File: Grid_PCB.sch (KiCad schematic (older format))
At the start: 9 parts, among them J10 LED_Conn, J11 ESP_Conn, J9 ESP_Conn, U1 SN74HC151N

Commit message: minor fix to mux strobe (enable) pin
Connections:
- net GND: now also U1.7 (~G)
- no-connect marks 2 -> 1
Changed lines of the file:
@@
 Wire Wire Line
 	4150 1500 4650 1500
-$Comp
-L grid:SN74HC151N U1
-U 1 1 61544325
-P 5500 4900
-F 0 "U1" H 5500 5475 50  0000 C CNN
-F 1 "SN74HC151N" H 5500 5384 50  0000 C CNN
-F 2 "Package_DIP:DIP-16_W10.16mm" H 5550 4900 50  0001 C CNN
-F 3 "https://www.ti.com/lit/ds/symlink/sn74hc151.pdf?ts=1632846774937&ref_url=https%253A%252F%252Fwww.google.com%252F" H 5550 4900 50  0001 C CNN
-	1    5500 4900
-	1    0    0    -1
-$EndComp
 Text Label 4800 4750 0    50   ~ 0
 BTN1
@@
 	1    0    0    -1
 $EndComp
-NoConn ~ 5200 5150
 $Comp
 L Device:C C9
@@
 	1    0    0    -1
 $EndComp
+$Comp
+L grid:SN74HC151N U1
+U 1 1 61544325
+P 5500 4900
+F 0 "U1" H 5500 5475 50  0000 C CNN
+F 1 "SN74HC151N" H 5500 5384 50  0000 C CNN
+F 2 "Package_DIP:DIP-16_W10.16mm" H 5550 4900 50  0001 C CNN
+F 3 "https://www.ti.com/lit/ds/symlink/sn74hc151.pdf?ts=1632846774937&ref_url=https%253A%252F%252Fwww.google.com%252F" H 5550 4900 50  0001 C CNN
+	1    5500 4900
+	1    0    0    -1
+$EndComp
+Wire Wire Line
+	5200 5150 5100 5150
+Wire Wire Line
+	5100 5150 5100 5250
+Connection ~ 5100 5250
 $EndSCHEMATC

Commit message: updated conns and mounting holes
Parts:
- J10, J11: footprint Connector_JST:JST_EH_B2B-EH-A_1x02_P2.50mm_Vertical -> conn:TE_640456-2
- J9: footprint Connector_JST:JST_EH_B5B-EH-A_1x05_P2.50mm_Vertical -> conn:TE_640456-5
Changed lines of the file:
@@
 F 0 "J10" H 8558 5131 50  0000 C CNN
 F 1 "LED_Conn" H 8558 5040 50  0000 C CNN
-F 2 "Connector_JST:JST_EH_B2B-EH-A_1x02_P2.50mm_Vertical" H 8450 4950 50  0001 C CNN
+F 2 "conn:TE_640456-2" H 8450 4950 50  0001 C CNN
 F 3 "~" H 8450 4950 50  0001 C CNN
 	1    8450 4950
@@
 F 0 "J9" H 1658 5081 50  0000 C CNN
 F 1 "ESP_Conn" H 1658 4990 50  0000 C CNN
-F 2 "Connector_JST:JST_EH_B5B-EH-A_1x05_P2.50mm_Vertical" H 1550 4600 50  0001 C CNN
+F 2 "conn:TE_640456-5" H 1550 4600 50  0001 C CNN
 F 3 "~" H 1550 4600 50  0001 C CNN
 	1    1550 4600
@@
 F 0 "J11" H 1858 6281 50  0000 C CNN
 F 1 "ESP_Conn" H 1858 6190 50  0000 C CNN
-F 2 "Connector_JST:JST_EH_B2B-EH-A_1x02_P2.50mm_Vertical" H 1750 5800 50  0001 C CNN
+F 2 "conn:TE_640456-2" H 1750 5800 50  0001 C CNN
 F 3 "~" H 1750 5800 50  0001 C CNN
 	1    1750 5800

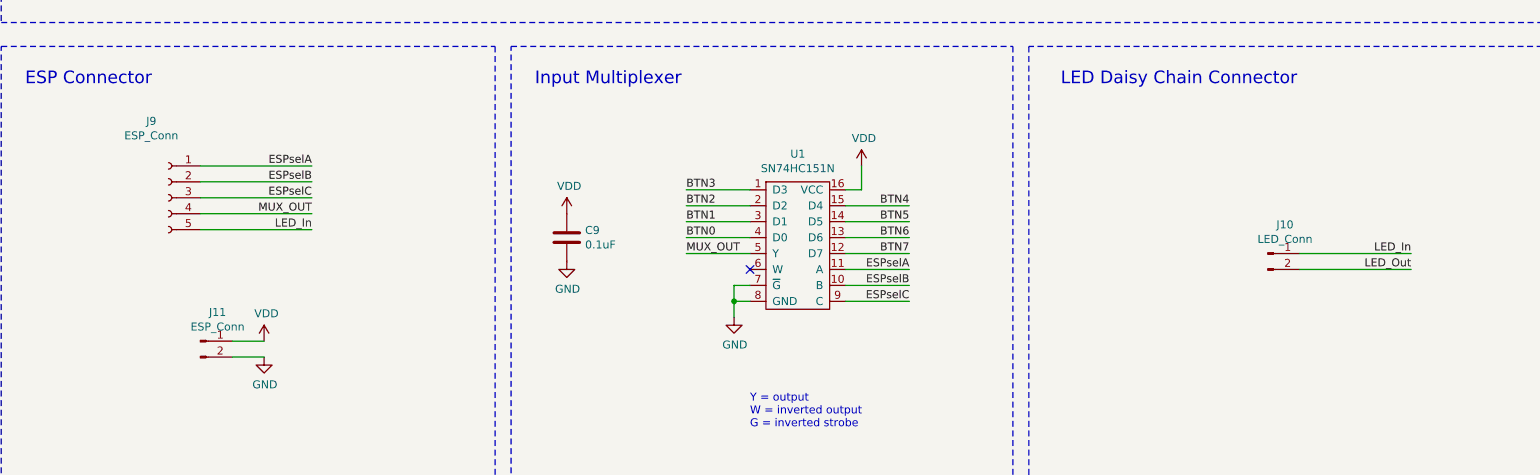
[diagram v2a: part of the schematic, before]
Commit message: updated jst footprint/library and updated routing on sel signals
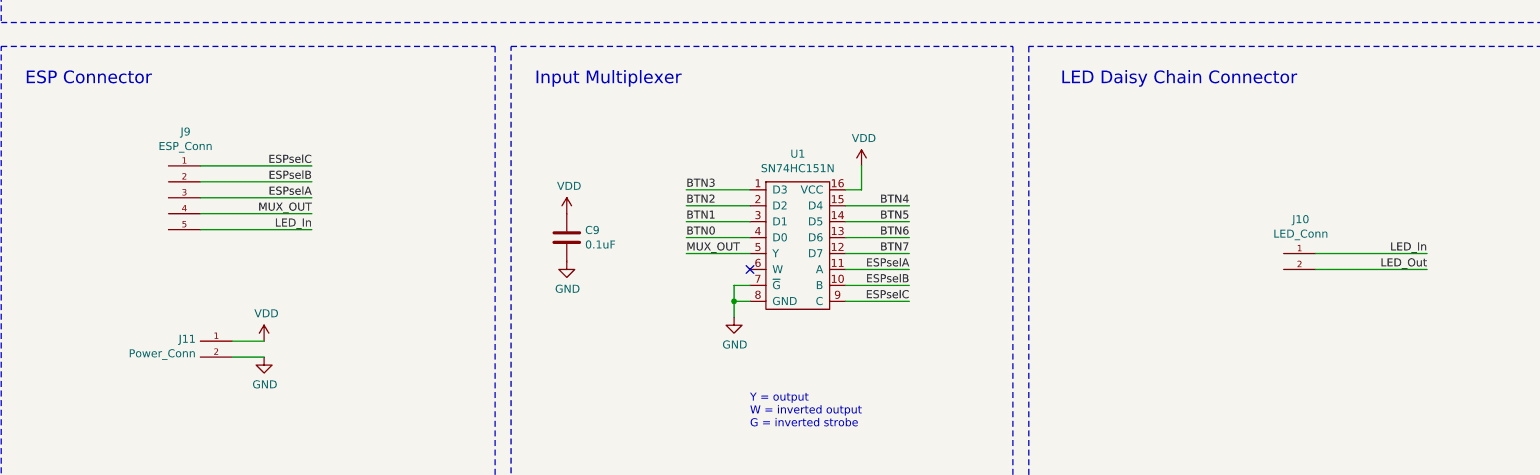
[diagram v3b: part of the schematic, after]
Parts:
- removed J10: LED_Conn, conn:TE_640456-2, symbol Connector:Conn_01x02_Male
- removed J11: ESP_Conn, conn:TE_640456-2, symbol grid:ESP_Conn
- removed J9: ESP_Conn, conn:TE_640456-5, symbol Connector:Conn_01x05_Female
- added J10: LED_Conn, JST_Conn:TE_640456-2, symbol JST_Conn:640456-2
- added J11: Power_Conn, JST_Conn:TE_640456-2, symbol JST_Conn:640456-2
- added J9: ESP_Conn, JST_Conn:TE_640456-5, symbol JST_Conn:640456-5
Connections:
- net ESPselA: now also J9.3
- net ESPselB: now also J9.2
- net ESPselC: now also J9.1
- net GND: now also J11.2
- net LED_In: now also J10.1, J9.5
- net LED_Out: now also J10.2
- net MUX_OUT: now also J9.4
- net VDD: now also J11.1
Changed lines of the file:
@@
 Text Label 2450 4700 2    50   ~ 0
 MUX_OUT
+Text Label 2450 4600 2    50   ~ 0
+ESPselA
 Text Label 2450 4400 2    50   ~ 0
-ESPselA
-Text Label 2450 4600 2    50   ~ 0
 ESPselC
 Text Label 2450 4500 2    50   ~ 0
 ESPselB
 Wire Wire Line
+	1750 4600 2450 4600
+Wire Wire Line
+	2450 4500 1750 4500
+Wire Wire Line
 	1750 4400 2450 4400
-Wire Wire Line
-	2450 4500 1750 4500
-Wire Wire Line
-	1750 4600 2450 4600
 Text Label 2450 4800 2    50   ~ 0
 LED_In
 Wire Wire Line
 	1750 4800 2450 4800
-$Comp
-L Connector:Conn_01x02_Male J10
-U 1 1 615862D5
-P 8450 4950
-F 0 "J10" H 8558 5131 50  0000 C CNN
-F 1 "LED_Conn" H 8558 5040 50  0000 C CNN
-F 2 "conn:TE_640456-2" H 8450 4950 50  0001 C CNN
-F 3 "~" H 8450 4950 50  0001 C CNN
-	1    8450 4950
-	1    0    0    -1
-$EndComp
-Wire Wire Line
-	8650 4950 9350 4950
-Text Label 9350 4950 2    50   ~ 0
+Wire Wire Line
+	8750 4950 9450 4950
+Text Label 9450 4950 2    50   ~ 0
 LED_In
 Wire Wire Line
-	8650 5050 9350 5050
-Text Label 9350 5050 2    50   ~ 0
+	8750 5050 9450 5050
+Text Label 9450 5050 2    50   ~ 0
 LED_Out
 Wire Wire Line
@@
 Wire Wire Line
 	1950 5600 2150 5600
-$Comp
-L Connector:Conn_01x05_Female J9
-U 1 1 6159E326
-P 1550 4600
-F 0 "J9" H 1658 5081 50  0000 C CNN
-F 1 "ESP_Conn" H 1658 4990 50  0000 C CNN
-F 2 "conn:TE_640456-5" H 1550 4600 50  0001 C CNN
-F 3 "~" H 1550 4600 50  0001 C CNN
-	1    1550 4600
-	-1   0    0    -1
-$EndComp
 $Comp
 L Mechanical:MountingHole H1
@@
 	500  6550 500  7750
 $Comp
-L grid:ESP_Conn J11
-U 1 1 6286F02E
-P 1750 5800
-F 0 "J11" H 1858 6281 50  0000 C CNN
-F 1 "ESP_Conn" H 1858 6190 50  0000 C CNN
-F 2 "conn:TE_640456-2" H 1750 5800 50  0001 C CNN
-F 3 "~" H 1750 5800 50  0001 C CNN
-	1    1750 5800
-	1    0    0    -1
-$EndComp
-$Comp
 L Device:C C9
 U 1 1 61664AB9
@@
 	5100 5150 5100 5250
 Connection ~ 5100 5250
+$Comp
+L JST_Conn:640456-2 J10
+U 1 1 616EEEF6
+P 8650 5050
+F 0 "J10" H 8643 5364 50  0000 C CNN
+F 1 "LED_Conn" H 8643 5273 50  0000 C CNN
+F 2 "JST_Conn:TE_640456-2" H 8450 4950 50  0001 L BNN
+F 3 "" H 8650 5050 50  0001 L BNN
+	1    8650 5050
+	-1   0    0    -1
+$EndComp
+$Comp
+L JST_Conn:640456-5 J9
+U 1 1 616F4C63
+P 1650 4600
+F 0 "J9" H 1643 5014 50  0000 C CNN
+F 1 "ESP_Conn" H 1643 4923 50  0000 C CNN
+F 2 "JST_Conn:TE_640456-5" H 1400 4300 50  0001 L BNN
+F 3 "" H 1650 4600 50  0001 L BNN
+	1    1650 4600
+	-1   0    0    -1
+$EndComp
+$Comp
+L JST_Conn:640456-2 J11
+U 1 1 616F6072
+P 1850 5600
+F 0 "J11" H 1979 5713 50  0000 L CNN
+F 1 "Power_Conn" H 1979 5622 50  0000 L CNN
+F 2 "JST_Conn:TE_640456-2" H 1650 5500 50  0001 L BNN
+F 3 "" H 1850 5600 50  0001 L BNN
+	1    1850 5600
+	-1   0    0    -1
+$EndComp
 $EndSCHEMATC

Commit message: updated hole footprint
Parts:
- H1, H2, H3, H4: footprint MountingHole:MountingHole_3.2mm_M3 -> grid:MountingHole_3.2mm_M3
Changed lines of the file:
@@
 F 0 "H1" H 2850 7046 50  0000 L CNN
 F 1 "MountingHole" H 2850 6955 50  0000 L CNN
-F 2 "MountingHole:MountingHole_3.2mm_M3" H 2750 7000 50  0001 C CNN
+F 2 "grid:MountingHole_3.2mm_M3" H 2750 7000 50  0001 C CNN
 F 3 "https://www.digikey.com/en/products/detail/essentra-components/50M030050F012/11639328~" H 2750 7000 50  0001 C CNN
 	1    2750 7000
@@
 F 0 "H2" H 2850 7296 50  0000 L CNN
 F 1 "MountingHole" H 2850 7205 50  0000 L CNN
-F 2 "MountingHole:MountingHole_3.2mm_M3" H 2750 7250 50  0001 C CNN
+F 2 "grid:MountingHole_3.2mm_M3" H 2750 7250 50  0001 C CNN
 F 3 "https://www.digikey.com/en/products/detail/essentra-components/50M030050F012/11639328~" H 2750 7250 50  0001 C CNN
 	1    2750 7250
@@
 F 0 "H3" H 3650 7046 50  0000 L CNN
 F 1 "MountingHole" H 3650 6955 50  0000 L CNN
-F 2 "MountingHole:MountingHole_3.2mm_M3" H 3550 7000 50  0001 C CNN
+F 2 "grid:MountingHole_3.2mm_M3" H 3550 7000 50  0001 C CNN
 F 3 "https://www.digikey.com/en/products/detail/essentra-components/50M030050F012/11639328~" H 3550 7000 50  0001 C CNN
 	1    3550 7000
@@
 F 0 "H4" H 3650 7296 50  0000 L CNN
 F 1 "MountingHole" H 3650 7205 50  0000 L CNN
-F 2 "MountingHole:MountingHole_3.2mm_M3" H 3550 7250 50  0001 C CNN
+F 2 "grid:MountingHole_3.2mm_M3" H 3550 7250 50  0001 C CNN
 F 3 "https://www.digikey.com/en/products/detail/essentra-components/50M030050F012/11639328~" H 3550 7250 50  0001 C CNN
 	1    3550 7250
